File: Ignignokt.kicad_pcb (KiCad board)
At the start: 2 copper layers, 324 x 356 mm, 264 parts, among them J1 Barrel_Jack_Switch, J2 Conn_01x02_Pin, Q1 IRLB8721PBF, Q2 FQP27P06, U1 LM2585S-12, U2 LM2937ET-5.0, U3 PIC12F675-IMC

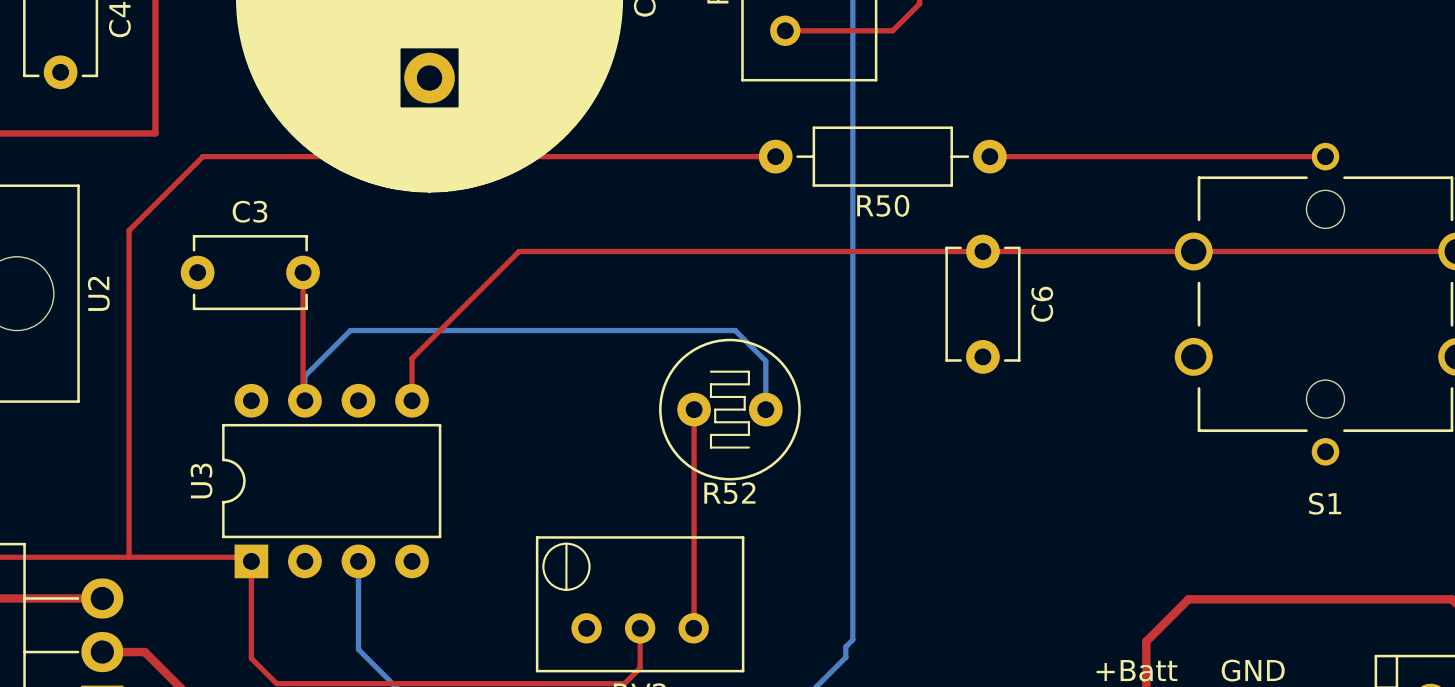
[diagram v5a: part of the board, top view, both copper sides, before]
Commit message: Some minor tweaks
Moved the button light to between the light and ground instread of between power and the light. Cleaned up the schematic somewhat.

Signed-off-by: Nathan Hjelm <hjelmn@me.com>
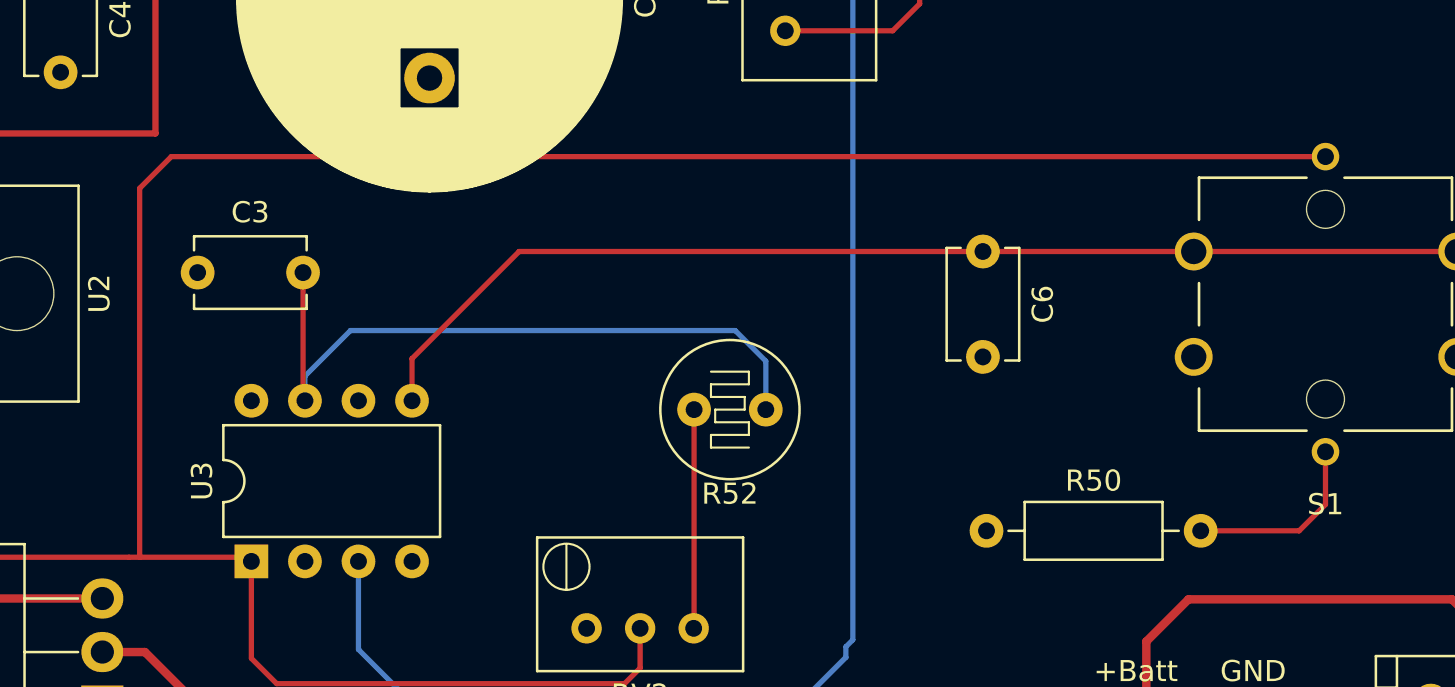
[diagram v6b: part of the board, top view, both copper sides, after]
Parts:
- moved R50 17.8 mm to (92.4, 354.2), turned to 0 degrees
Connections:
- R50 pad 1: Net-(R50-Pad1) -> GND
- R50 pad 2: +5V -> Net-(R50-Pad2)
- S1 pad E: Net-(R50-Pad1) -> +5V
- S1 pad F: GND -> Net-(R50-Pad2)
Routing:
- net +5V: track 113.5 -> 140.2 mm
- net Net-(R50-Pad1): track 15.9 -> 0.00 mm
- net Net-(R50-Pad2): track 0.00 -> 8.94 mm
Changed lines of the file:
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@@
   (net 202 "Net-(LED182-A)")
   (net 203 "Net-(LED184-A)")
-  (net 204 "Net-(R50-Pad1)")
-  (net 205 "Net-(R52-Pad2)")
-  (net 206 "Net-(LED21-K)")
-  (net 207 "unconnected-(RV1-Pad1)")
-  (net 208 "unconnected-(RV2-Pad1)")
+  (net 204 "Net-(R52-Pad2)")
+  (net 205 "Net-(LED21-K)")
+  (net 206 "unconnected-(RV1-Pad1)")
+  (net 207 "unconnected-(RV2-Pad1)")
+  (net 208 "Net-(R50-Pad2)")
   (footprint "LED_THT:LED_D10.0mm" (layer "F.Cu")
     (at 142.09 201.33)
@@
       (net 1 "GND") (pintype "passive") (solder_mask_margin 0.102))
     (pad "E" thru_hole circle (at -7 0 270) (size 1.308 1.308) (drill 0.8) (layers "*.Cu" "*.Mask")
-      (net 204 "Net-(R50-Pad1)") (pintype "passive") (solder_mask_margin 0.102))
+      (net 79 "+5V") (pintype "passive") (solder_mask_margin 0.102))
     (pad "F" thru_hole circle (at 7 0 270) (size 1.308 1.308) (drill 0.8) (layers "*.Cu" "*.Mask")
-      (net 1 "GND") (pintype "passive") (solder_mask_margin 0.102))
+      (net 208 "Net-(R50-Pad2)") (pintype "passive") (solder_mask_margin 0.102))
   )
   (footprint "Capacitor_THT:CP_Radial_D18.0mm_P7.50mm" (layer "F.Cu")
@@
       (stroke (width 0.1) (type solid)) (fill none) (layer "F.Fab"))
     (pad "1" thru_hole rect (at 1.27 -1.27 270) (size 1.8 1.8) (drill 0.9) (layers "*.Cu" "*.Mask")
-      (net 206 "Net-(LED21-K)") (pinfunction "K") (pintype "passive"))
+      (net 205 "Net-(LED21-K)") (pinfunction "K") (pintype "passive"))
     (pad "2" thru_hole circle (at 1.27 1.27 270) (size 1.8 1.8) (drill 0.9) (layers "*.Cu" "*.Mask")
       (net 95 "Net-(LED105-A)") (pinfunction "A") (pintype "passive"))
@@
       (stroke (width 0.1) (type solid)) (layer "F.Fab"))
     (pad "1" thru_hole circle (at 0 0 90) (size 1.44 1.44) (drill 0.8) (layers "*.Cu" "*.Mask")
-      (net 207 "unconnected-(RV1-Pad1)") (pinfunction "1") (pintype "passive"))
+      (net 206 "unconnected-(RV1-Pad1)") (pinfunction "1") (pintype "passive"))
     (pad "2" thru_hole circle (at -2.54 0 90) (size 1.44 1.44) (drill 0.8) (layers "*.Cu" "*.Mask")
       (net 30 "+12V") (pinfunction "2") (pintype "passive"))
@@
       (net 2 "Net-(U3-GP0)") (pintype "passive"))
     (pad "2" thru_hole circle (at 3.4 0 180) (size 1.6 1.6) (drill 0.8) (layers "*.Cu" "*.Mask")
-      (net 205 "Net-(R52-Pad2)") (pintype "passive"))
+      (net 204 "Net-(R52-Pad2)") (pintype "passive"))
     (model "${KICAD6_3DMODEL_DIR}/OptoDevice.3dshapes/R_LDR_D6.4mm_P3.4mm_Vertical.wrl"
       (offset (xyz 0 0 0))
@@
   )
   (footprint "Resistor_THT:R_Axial_DIN0207_L6.3mm_D2.5mm_P10.16mm_Horizontal" (layer "F.Cu")
-    (at 92.58 336.5 180)
+    (at 92.42 354.25)
     (descr "Resistor, Axial_DIN0207 series, Axial, Horizontal, pin pitch=10.16mm, 0.25W = 1/4W, length*diameter=6.3*2.5mm^2, http://cdn-reichelt.de/documents/datenblatt/B400/1_4W%23YAG.pdf")
     (tags "Resistor Axial_DIN0207 series Axial Horizontal pin pitch 10.16mm 0.25W = 1/4W length 6.3mm diameter 2.5mm")
@@
     (fp_line (start 10.16 0) (end 8.23 0)
       (stroke (width 0.1) (type solid)) (layer "F.Fab"))
-    (pad "1" thru_hole circle (at 0 0 180) (size 1.6 1.6) (drill 0.8) (layers "*.Cu" "*.Mask")
-      (net 204 "Net-(R50-Pad1)") (pintype "passive"))
-    (pad "2" thru_hole oval (at 10.16 0 180) (size 1.6 1.6) (drill 0.8) (layers "*.Cu" "*.Mask")
-      (net 79 "+5V") (pintype "passive"))
+    (pad "1" thru_hole circle (at 0 0) (size 1.6 1.6) (drill 0.8) (layers "*.Cu" "*.Mask")
+      (net 1 "GND") (pintype "passive"))
+    (pad "2" thru_hole oval (at 10.16 0) (size 1.6 1.6) (drill 0.8) (layers "*.Cu" "*.Mask")
+      (net 208 "Net-(R50-Pad2)") (pintype "passive"))
     (model "${KICAD6_3DMODEL_DIR}/Resistor_THT.3dshapes/R_Axial_DIN0207_L6.3mm_D2.5mm_P10.16mm_Horizontal.wrl"
       (offset (xyz 0 0 0))
@@
       (net 34 "Net-(LED22-K)") (pinfunction "K") (pintype "passive"))
     (pad "2" thru_hole circle (at 1.27 1.27 270) (size 1.8 1.8) (drill 0.9) (layers "*.Cu" "*.Mask")
-      (net 206 "Net-(LED21-K)") (pinfunction "A") (pintype "passive"))
+      (net 205 "Net-(LED21-K)") (pinfunction "A") (pintype "passive"))
     (model "${KICAD6_3DMODEL_DIR}/LED_THT.3dshapes/LED_D10.0mm.wrl"
       (offset (xyz 0 0 0))
@@
       (stroke (width 0.1) (type solid)) (layer "F.Fab"))
     (pad "1" thru_hole circle (at 0 0 180) (size 1.44 1.44) (drill 0.8) (layers "*.Cu" "*.Mask")
-      (net 208 "unconnected-(RV2-Pad1)") (pinfunction "1") (pintype "passive"))
+      (net 207 "unconnected-(RV2-Pad1)") (pinfunction "1") (pintype "passive"))
     (pad "2" thru_hole circle (at -2.54 0 180) (size 1.44 1.44) (drill 0.8) (layers "*.Cu" "*.Mask")
       (net 79 "+5V") (pinfunction "2") (pintype "passive"))
     (pad "3" thru_hole circle (at -5.08 0 180) (size 1.44 1.44) (drill 0.8) (layers "*.Cu" "*.Mask")
-      (net 205 "Net-(R52-Pad2)") (pinfunction "3") (pintype "passive"))
+      (net 204 "Net-(R52-Pad2)") (pinfunction "3") (pintype "passive"))
     (model "${KICAD6_3DMODEL_DIR}/Potentiometer_THT.3dshapes/Potentiometer_Bourns_3299W_Vertical.wrl"
       (offset (xyz 0 0 0))
@@
   (segment (start 100 363.5) (end 56 363.5) (width 0.4) (layer "F.Cu") (net 78))
   (segment (start 58.75 361.5) (end 57.55 360.3) (width 0.25) (layer "F.Cu") (net 79))
+  (segment (start 53.75 336.5) (end 52.25 338) (width 0.25) (layer "F.Cu") (net 79))
   (segment (start 29.77 349.77) (end 35.503249 355.503249) (width 0.25) (layer "F.Cu") (net 79))
   (segment (start 75.25 361.5) (end 58.75 361.5) (width 0.25) (layer "F.Cu") (net 79))
-  (segment (start 55.25 336.5) (end 51.75 340) (width 0.25) (layer "F.Cu") (net 79))
-  (segment (start 51.75 355.503249) (end 57.075 355.503249) (width 0.25) (layer "F.Cu") (net 79))
-  (segment (start 51.75 340) (end 51.75 355.503249) (width 0.25) (layer "F.Cu") (net 79))
+  (segment (start 52.25 355.503249) (end 57.075 355.503249) (width 0.25) (layer "F.Cu") (net 79))
+  (segment (start 51.75 355.503249) (end 52.25 355.503249) (width 0.25) (layer "F.Cu") (net 79))
+  (segment (start 52.25 338) (end 52.25 355.503249) (width 0.25) (layer "F.Cu") (net 79))
   (segment (start 23.5 345.5) (end 29.73 345.5) (width 0.25) (layer "F.Cu") (net 79))
   (segment (start 29.77 345.54) (end 29.77 349.77) (width 0.25) (layer "F.Cu") (net 79))
+  (segment (start 108.5 336.5) (end 53.75 336.5) (width 0.25) (layer "F.Cu") (net 79))
   (segment (start 75.99 358.875) (end 75.99 360.76) (width 0.25) (layer "F.Cu") (net 79))
   (segment (start 75.99 360.76) (end 75.25 361.5) (width 0.25) (layer "F.Cu") (net 79))
   (segment (start 35.503249 355.503249) (end 51.75 355.503249) (width 0.25) (layer "F.Cu") (net 79))
   (segment (start 57.55 360.3) (end 57.55 355.7) (width 0.25) (layer "F.Cu") (net 79))
-  (segment (start 82.42 336.5) (end 55.25 336.5) (width 0.25) (layer "F.Cu") (net 79))
   (segment (start 128.07 26.07) (end 135.74 26.07) (width 0.3) (layer "F.Cu") (net 80))
   (segment (start 123.04 23.53) (end 125.53 23.53) (width 0.3) (layer "F.Cu") (net 80))
@@
   (segment (start 251.68 302.93) (end 250.04 302.93) (width 0.25) (layer "F.Cu") (net 203))
   (segment (start 252.08 318.17) (end 253 317.25) (width 0.25) (layer "F.Cu") (net 203))
-  (segment (start 92.58 336.5) (end 108.5 336.5) (width 0.25) (layer "F.Cu") (net 204))
-  (segment (start 78.55 358.855) (end 78.53 358.875) (width 0.25) (layer "F.Cu") (net 205))
-  (segment (start 78.55 348.5) (end 78.55 358.855) (width 0.25) (layer "F.Cu") (net 205))
-  (segment (start 164.38 61.63) (end 166.92 64.17) (width 0.25) (layer "F.Cu") (net 206))
-  (segment (start 161.14 61.63) (end 164.38 61.63) (width 0.25) (layer "F.Cu") (net 206))
-  (segment (start 166.92 64.17) (end 173.84 64.17) (width 0.25) (layer "F.Cu") (net 206))
+  (segment (start 78.55 358.855) (end 78.53 358.875) (width 0.25) (layer "F.Cu") (net 204))
+  (segment (start 78.55 348.5) (end 78.55 358.855) (width 0.25) (layer "F.Cu") (net 204))
+  (segment (start 164.38 61.63) (end 166.92 64.17) (width 0.25) (layer "F.Cu") (net 205))
+  (segment (start 161.14 61.63) (end 164.38 61.63) (width 0.25) (layer "F.Cu") (net 205))
+  (segment (start 166.92 64.17) (end 173.84 64.17) (width 0.25) (layer "F.Cu") (net 205))
+  (segment (start 108.5 353) (end 107.25 354.25) (width 0.25) (layer "F.Cu") (net 208))
+  (segment (start 108.5 350.5) (end 108.5 353) (width 0.25) (layer "F.Cu") (net 208))
+  (segment (start 107.25 354.25) (end 102.58 354.25) (width 0.25) (layer "F.Cu") (net 208))
   (zone (net 1) (net_name "GND") (layer "B.Cu") (name "Ground") (hatch edge 0.5)
     (connect_pads (clearance 0.5))
